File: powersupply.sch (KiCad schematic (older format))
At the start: 0 parts

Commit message: blub
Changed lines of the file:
@@
 $Descr A3 16535 11693
 encoding utf-8
-Sheet 4 12
+Sheet 4 13
 Title ""
 Date ""
@@
 $EndSheet
 Wire Wire Line
-	3125 1625 3375 1625
+	3125 1625 3725 1625
 Wire Wire Line
-	3375 1625 3725 1625
-Wire Wire Line
-	3125 1775 3225 1775
-Wire Wire Line
-	3225 1775 3725 1775
+	3125 1775 3725 1775
 Wire Wire Line
 	3725 2775 3375 2775
@@
 	3725 2025 3650 2025
 Wire Bus Line
-	3550 2050 3550 2125
-Wire Bus Line
-	3550 2125 3550 3300
-Wire Bus Line
-	3550 3300 3550 3375
-Wire Bus Line
-	3550 3375 3550 3650
+	3550 2050 3550 3650
 Entry Wire Line
 	3550 3300 3650 3200
@@
 GND
 Wire Wire Line
-	5075 2850 5350 2850
-Wire Wire Line
-	5350 2850 5525 2850
+	5075 2850 5525 2850
 Wire Wire Line
 	5525 2950 5075 2950
 Wire Wire Line
-	5075 3075 5250 3075
-Wire Wire Line
-	5250 3075 5525 3075
+	5075 3075 5525 3075
 Wire Wire Line
 	5075 2375 5250 2375
@@
 $EndSheet
 Wire Wire Line
-	5075 1625 6725 1625
-Wire Wire Line
-	6725 1625 6875 1625
+	5075 1625 6875 1625
 Wire Wire Line
 	5075 1750 6875 1750

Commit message: daily commit
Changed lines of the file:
@@
 $EndSheet
 Wire Wire Line
-	3125 1625 3725 1625
+	3125 1625 3375 1625
 Wire Wire Line
-	3125 1775 3725 1775
+	3375 1625 3725 1625
+Wire Wire Line
+	3125 1775 3225 1775
+Wire Wire Line
+	3225 1775 3725 1775
 Wire Wire Line
 	3725 2775 3375 2775
@@
 	3725 2025 3650 2025
 Wire Bus Line
-	3550 2050 3550 3650
+	3550 2050 3550 2125
+Wire Bus Line
+	3550 2125 3550 3300
+Wire Bus Line
+	3550 3300 3550 3375
+Wire Bus Line
+	3550 3375 3550 3650
 Entry Wire Line
 	3550 3300 3650 3200
@@
 GND
 Wire Wire Line
-	5075 2850 5525 2850
+	5075 2850 5350 2850
+Wire Wire Line
+	5350 2850 5525 2850
 Wire Wire Line
 	5525 2950 5075 2950
 Wire Wire Line
-	5075 3075 5525 3075
+	5075 3075 5250 3075
+Wire Wire Line
+	5250 3075 5525 3075
 Wire Wire Line
 	5075 2375 5250 2375
@@
 $EndSheet
 Wire Wire Line
-	5075 1625 6875 1625
+	5075 1625 6725 1625
+Wire Wire Line
+	6725 1625 6875 1625
 Wire Wire Line
 	5075 1750 6875 1750
@@
 Connection ~ 6725 1625
 Wire Wire Line
-	5075 1825 6625 1825
+	5075 1825 6650 1825
 Wire Wire Line
-	6625 1825 6625 2350
+	6650 1825 6650 2350
 Wire Wire Line
-	6625 2350 6875 2350
+	6650 2350 6875 2350
 $EndSCHEMATC

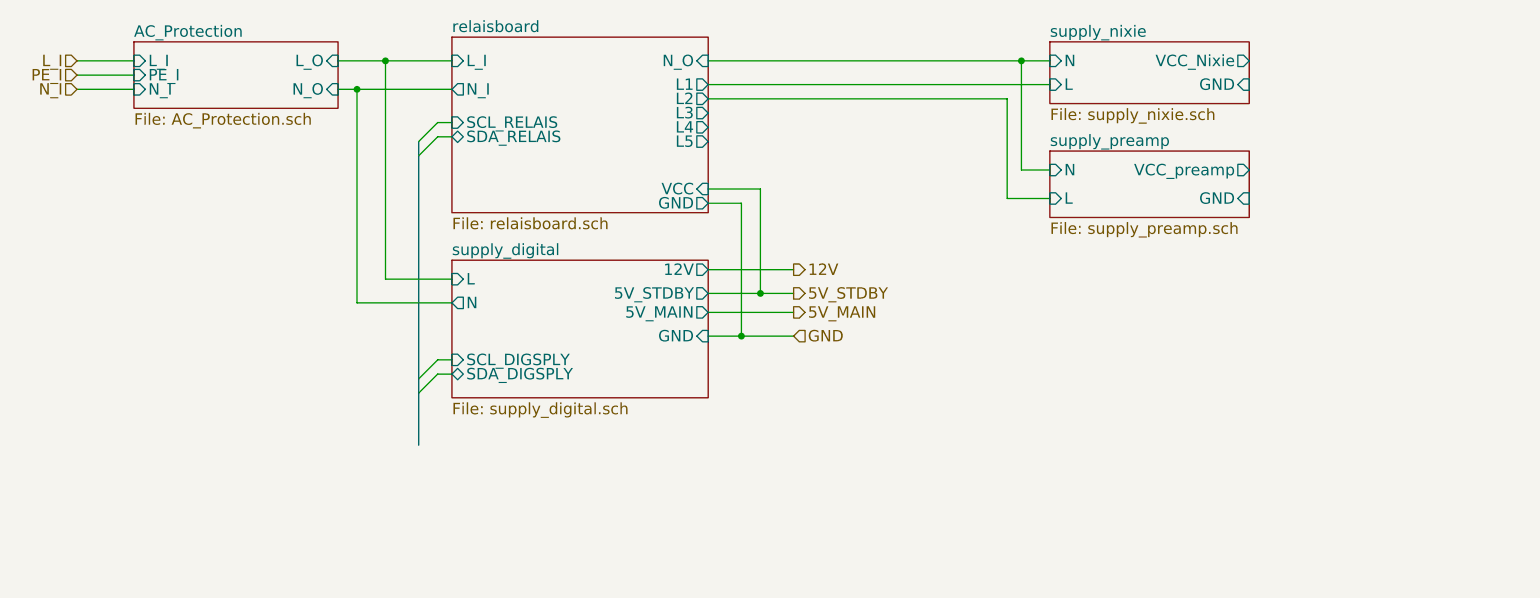
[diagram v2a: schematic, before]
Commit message: phono_preamp and more
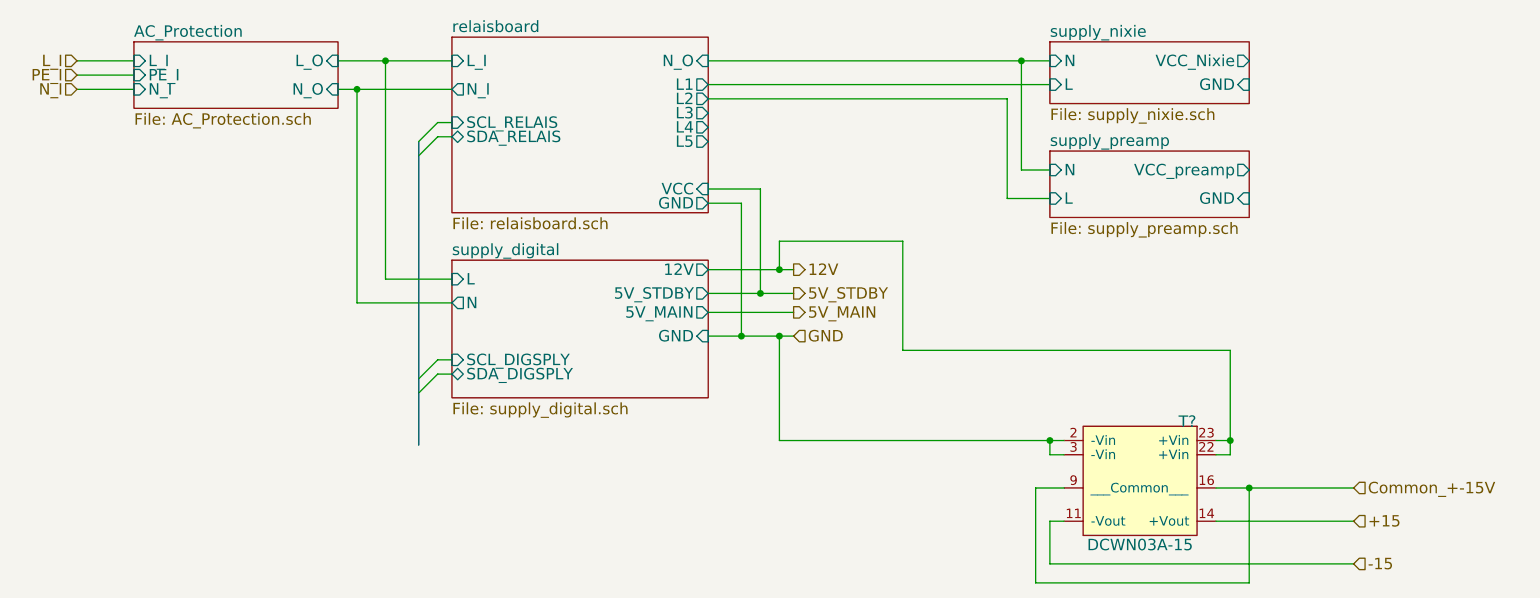
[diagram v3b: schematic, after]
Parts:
- added T?: DCWN03A-15, symbol DCWN03A-15
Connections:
- net 12V: now also T?.22 (+Vin), T?.23 (+Vin)
- net GND: now also T?.2 (-Vin), T?.3 (-Vin)
- new net +15: T?.14 (+Vout)
- new net -15: T?.11 (-Vout)
- new net Common_+-15V: T?.16, T?.9 (___Common___)
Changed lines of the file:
@@
 $Descr A3 16535 11693
 encoding utf-8
-Sheet 4 13
+Sheet 4 14
 Title ""
 Date ""
@@
 $EndSheet
 Wire Wire Line
-	3125 1625 3375 1625
-Wire Wire Line
-	3375 1625 3725 1625
-Wire Wire Line
-	3125 1775 3225 1775
-Wire Wire Line
-	3225 1775 3725 1775
+	3125 1625 3725 1625
+Wire Wire Line
+	3125 1775 3725 1775
 Wire Wire Line
 	3725 2775 3375 2775
@@
 	3725 2025 3650 2025
 Wire Bus Line
-	3550 2050 3550 2125
-Wire Bus Line
-	3550 2125 3550 3300
-Wire Bus Line
-	3550 3300 3550 3375
-Wire Bus Line
-	3550 3375 3550 3650
+	3550 2050 3550 3650
 Entry Wire Line
 	3550 3300 3650 3200
@@
 GND
 Wire Wire Line
-	5075 2850 5350 2850
-Wire Wire Line
-	5350 2850 5525 2850
+	5075 2850 5525 2850
 Wire Wire Line
 	5525 2950 5075 2950
 Wire Wire Line
-	5075 3075 5250 3075
-Wire Wire Line
-	5250 3075 5525 3075
+	5075 3075 5525 3075
 Wire Wire Line
 	5075 2375 5250 2375
@@
 $EndSheet
 Wire Wire Line
-	5075 1625 6725 1625
-Wire Wire Line
-	6725 1625 6875 1625
+	5075 1625 6875 1625
 Wire Wire Line
 	5075 1750 6875 1750
@@
 Wire Wire Line
 	6650 2350 6875 2350
+$Comp
+L DCWN03A-15 T?
+U 1 1 593B76FA
+P 7350 3800
+F 0 "T?" H 7100 4075 60  0000 C CNN
+F 1 "DCWN03A-15" H 7350 3425 60  0000 C CNN
+F 2 "" H 7325 3775 60  0001 C CNN
+F 3 "" H 7325 3775 60  0001 C CNN
+	1    7350 3800
+	-1   0    0    -1
+$EndComp
+Wire Wire Line
+	7825 3700 7750 3700
+Wire Wire Line
+	7825 3150 7825 3700
+Wire Wire Line
+	7825 3625 7750 3625
+Wire Wire Line
+	6950 3700 6875 3700
+Wire Wire Line
+	6875 3700 6875 3625
+Wire Wire Line
+	5450 3625 6950 3625
+Wire Wire Line
+	5450 3625 5450 3075
+Connection ~ 5450 3075
+Connection ~ 6875 3625
+Wire Wire Line
+	5450 2725 5450 2575
+Wire Wire Line
+	5450 2575 6100 2575
+Wire Wire Line
+	6100 2575 6100 3150
+Wire Wire Line
+	6100 3150 7825 3150
+Connection ~ 7825 3625
+Connection ~ 5450 2725
+Text HLabel 8475 3875 2    60   Input ~ 0
+Common_+-15V
+Text HLabel 8475 4050 2    60   Input ~ 0
++15
+Text HLabel 8475 4275 2    60   Input ~ 0
+-15
+Wire Wire Line
+	6950 4050 6875 4050
+Wire Wire Line
+	6875 4050 6875 4275
+Wire Wire Line
+	6875 4275 8475 4275
+Wire Wire Line
+	6950 3875 6800 3875
+Wire Wire Line
+	6800 3875 6800 4375
+Wire Wire Line
+	6800 4375 7925 4375
+Wire Wire Line
+	7925 4375 7925 3875
+Wire Wire Line
+	7750 3875 8475 3875
+Connection ~ 7925 3875
+Wire Wire Line
+	8475 4050 7750 4050
 $EndSCHEMATC

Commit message: daily commit. Added new ADC
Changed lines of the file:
@@
 $Descr A3 16535 11693
 encoding utf-8
-Sheet 4 14
+Sheet 4 15
 Title ""
 Date ""
@@
 S 3725 1500 1350 925
 U 58BA9A19
-F0 "relaisboard" 60
-F1 "relaisboard.sch" 60
+F0 "relaisboard_supply" 60
+F1 "relaisboard_supply.sch" 60
 F2 "L_I" I L 3725 1625 60
 F3 "N_I" O L 3725 1775 60
